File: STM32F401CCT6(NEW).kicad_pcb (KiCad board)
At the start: 2 copper layers, 52 x 23 mm, 37 parts, among them J1 USB_OTG, J2 Conn_02x03_Odd_Even, J3 Conn_01x20_des, J4 Conn_01x05_desc, J5 Conn_01x20, SW1 SW_Push, U1 MIC5219-3.3, U2 STM32F401CCT6, U3 USBLC6-2SC6, Y1 32.786K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

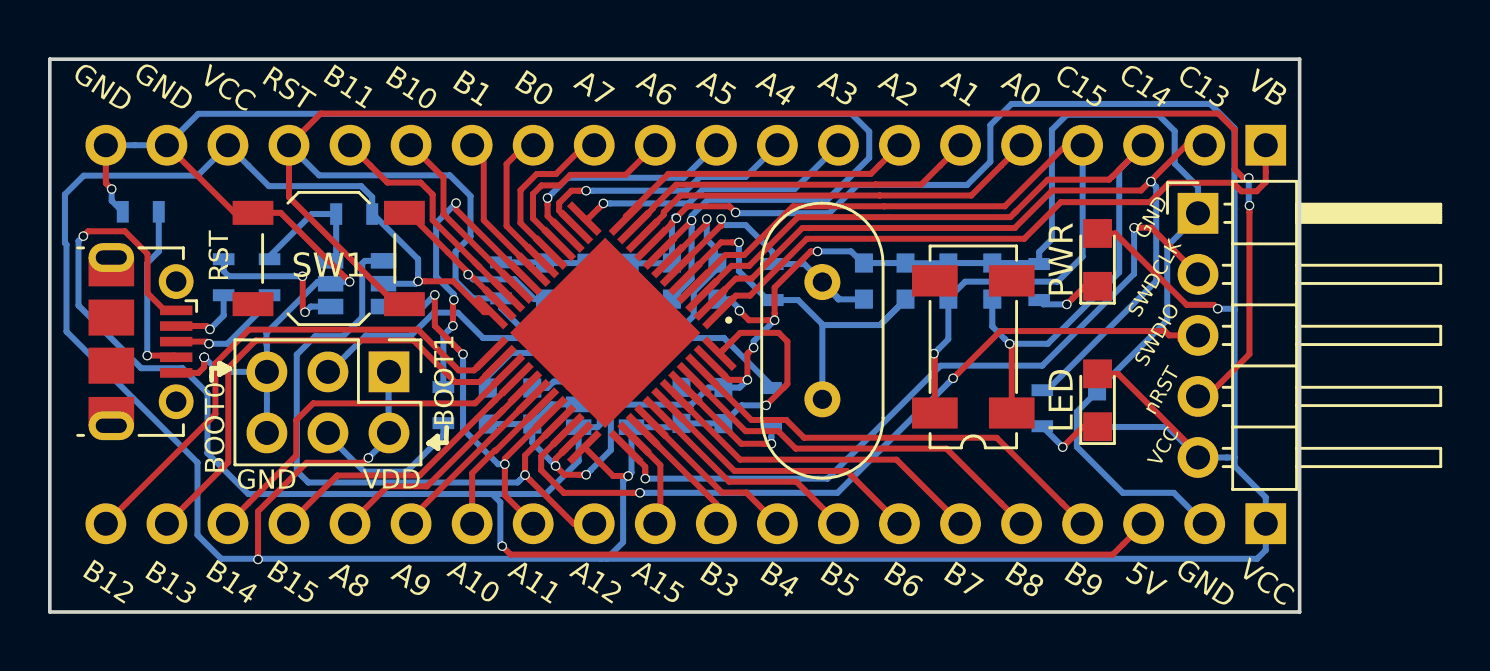
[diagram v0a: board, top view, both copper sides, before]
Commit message: Widen the track of power source
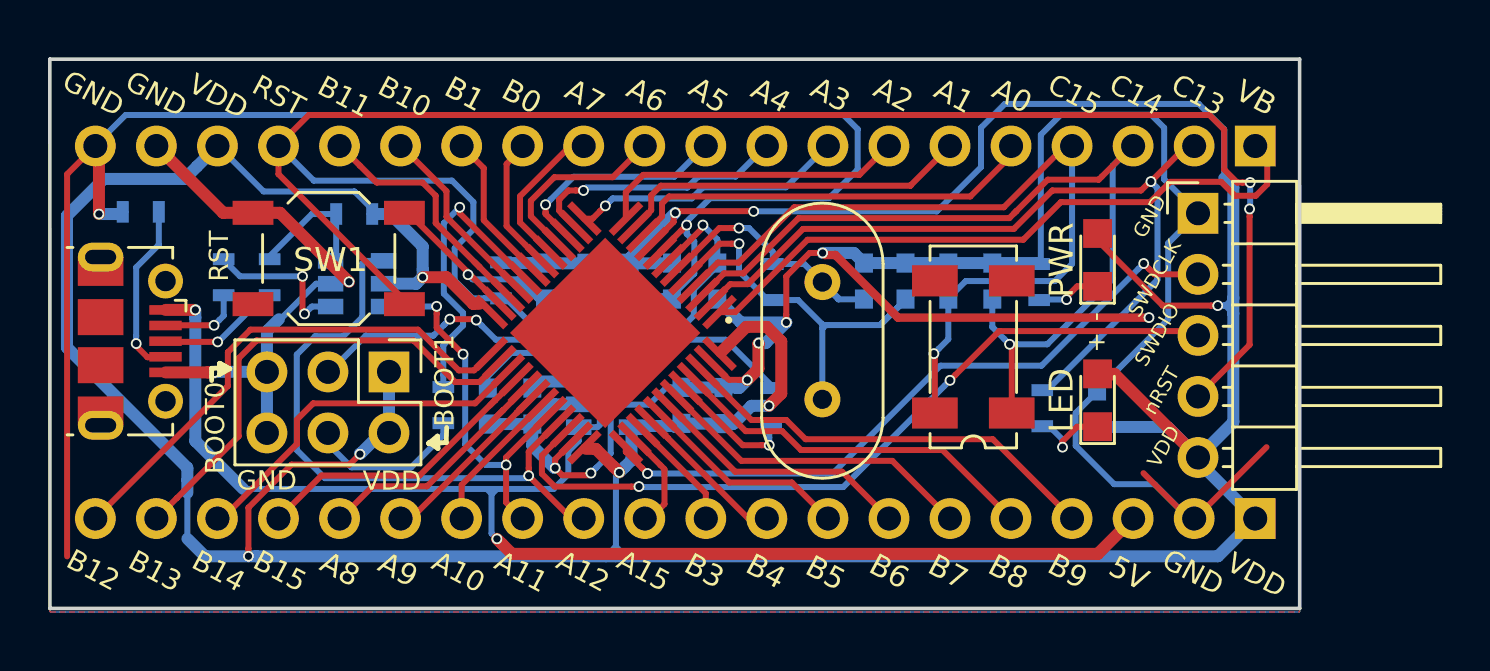
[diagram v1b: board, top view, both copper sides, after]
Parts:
- moved J5 0.49 mm to (123.9, 119.2)
- moved J1 0.44 mm to (76.2, 111.8)
- moved J3 0.44 mm to (123.9, 103.7)
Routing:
- net GND: track 162.7 -> 219.7 mm, vias 13 -> 12
- net +5V: track 72.0 -> 61.3 mm
- net VCC: track 193.2 -> 198.0 mm
- net /SWDCLK: track 31.2 -> 28.2 mm
- net /PA9: track 7.41 -> 9.05 mm
- net /PC15: track 35.3 -> 33.9 mm
- net /PC14: track 38.4 -> 37.4 mm
- net /PA12: track 27.7 -> 26.8 mm
- net /PA11: track 16.6 -> 15.9 mm
- net /SWDIO: track 33.4 -> 32.7 mm
- net /OSCOUT: track 11.7 -> 11.1 mm
- net /BOOT1: track 13.1 -> 12.5 mm, vias 3 -> 1
- net /PB4: track 7.01 -> 6.47 mm
- net /PB8: track 16.1 -> 15.6 mm
- net /PB6: track 11.7 -> 11.1 mm
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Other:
- board size 52 x 23 mm -> 52 x 22.9 mm
- net class Default: trace_width 0.25 -> 0.5
- net class new: trace_width 0.25 -> 0.5; via_dia 0.4 -> 0.45
- board text added: "+"
- board text added: "-"
- board text removed: "VCC"

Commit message: Added corner outline as an indicator for the footprint QFP48
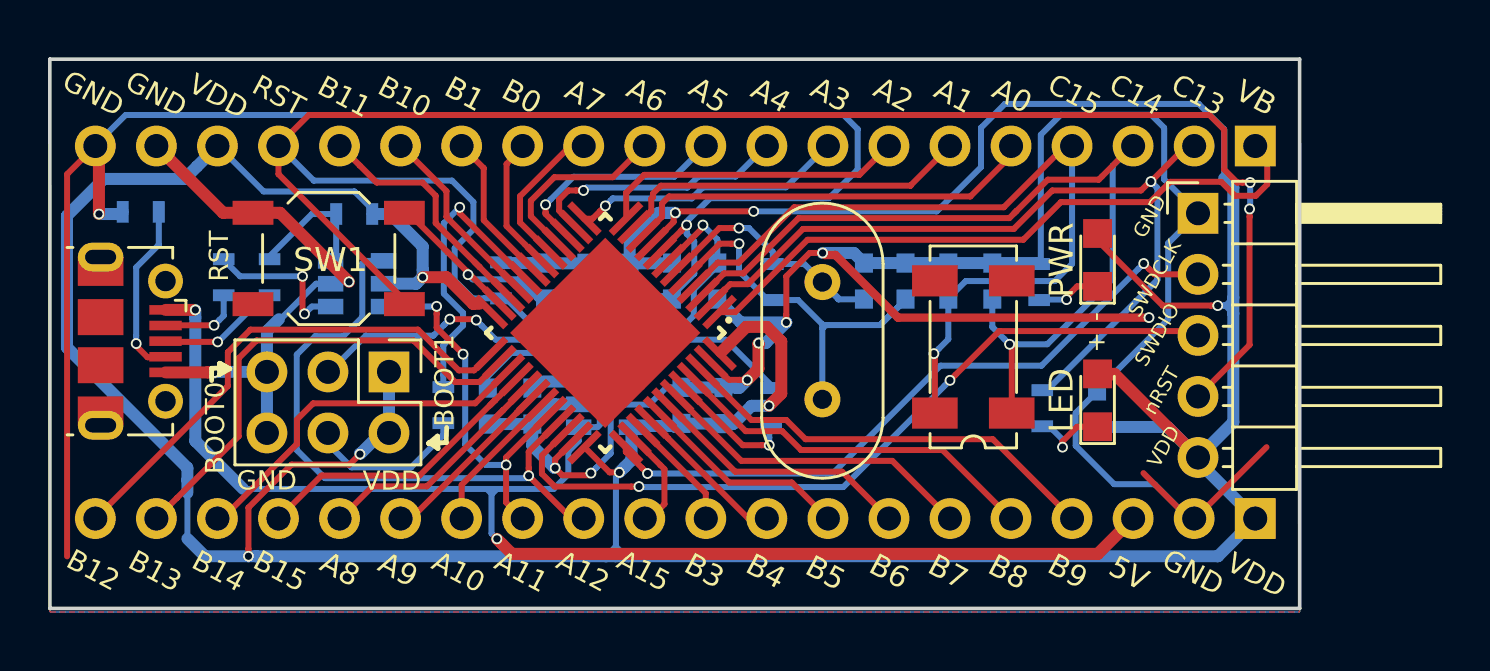
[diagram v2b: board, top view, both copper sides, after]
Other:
- net class Default: trace_width 0.5 -> 0.25
- net class new: trace_width 0.5 -> 0.25
